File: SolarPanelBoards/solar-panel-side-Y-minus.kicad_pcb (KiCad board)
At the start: 2 copper layers, 82 x 99 mm, 24 parts, among them J1 Conn_01x06, U1 OPT3001DNPT

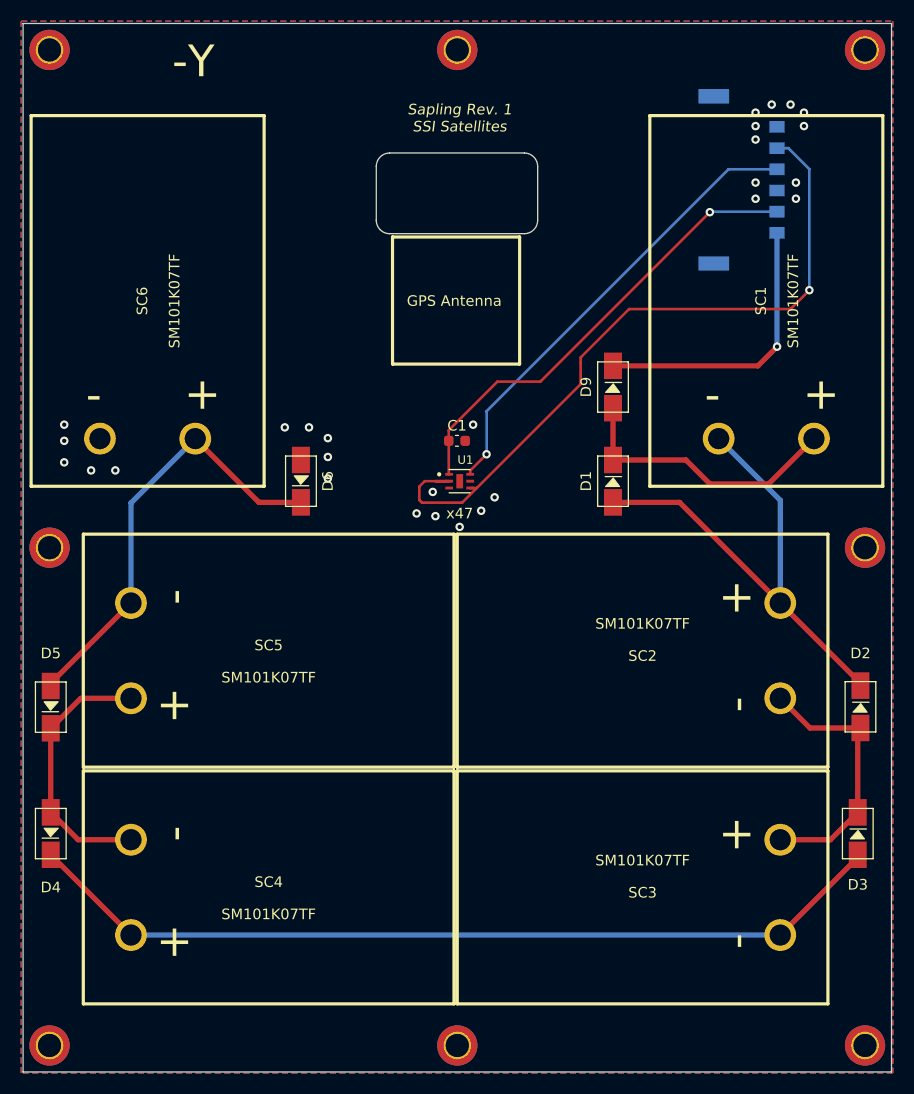
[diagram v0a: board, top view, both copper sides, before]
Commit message: Battery board and side panels ready for CAD check and review, pycubed not finished yet
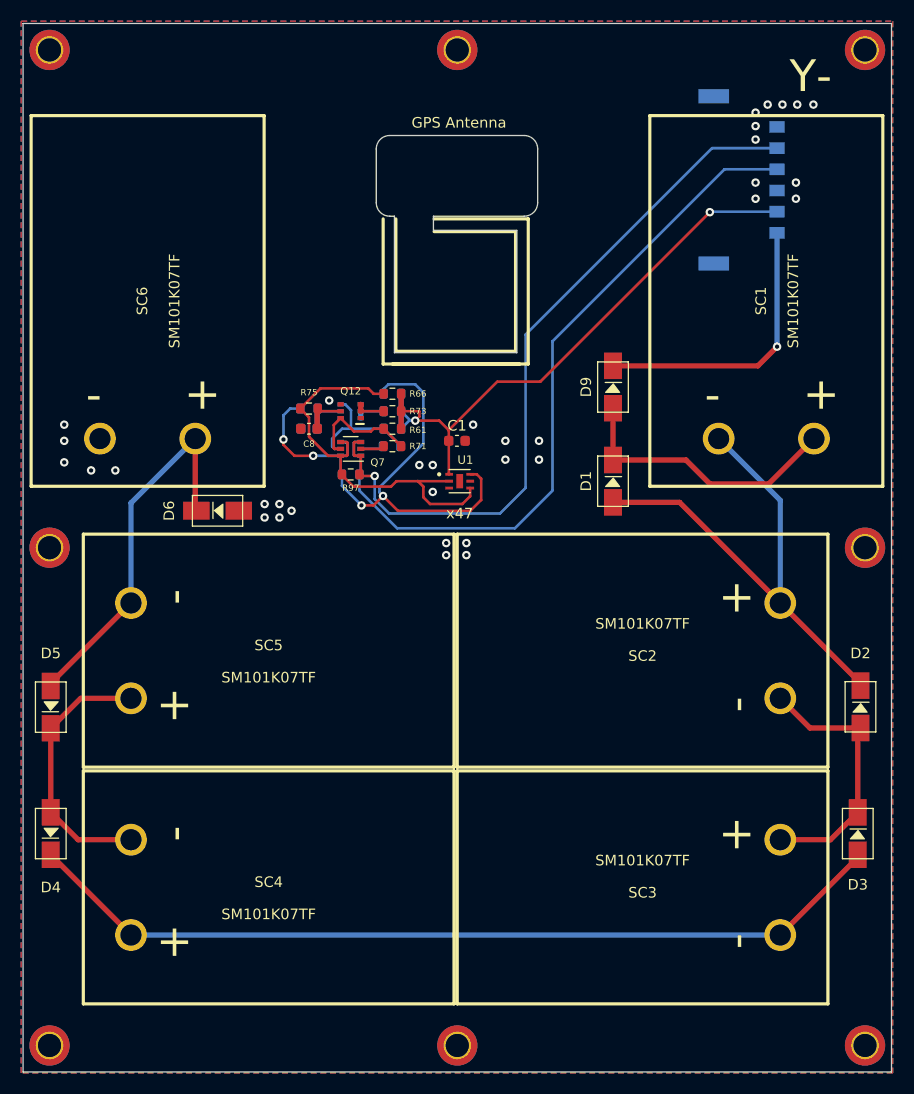
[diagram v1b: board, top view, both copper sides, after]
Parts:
- added C40: 10nF, Capacitor_SMD:C_0603_1608Metric, B.Cu at (133.3, 86.0)
- added C8: 10nF, Capacitor_SMD:C_0603_1608Metric, F.Cu at (133.3, 86.0)
- added Q12: BSS138DWQ-7, sapling:BSS138DWQ-7, F.Cu at (137.3, 84.3)
- added Q13: BSS138DWQ-7, sapling:BSS138DWQ-7, B.Cu at (137.3, 84.3)
- added Q7: MBT2222ADW1T1, Package_TO_SOT_SMD:SOT-363_SC-70-6, F.Cu at (137.3, 87.9)
- added Q8: MBT2222ADW1T1, Package_TO_SOT_SMD:SOT-363_SC-70-6, B.Cu at (137.3, 87.9)
- added R61: 10K, Resistor_SMD:R_0603_1608Metric, F.Cu at (141.2, 86.0)
- added R62: 10K, Resistor_SMD:R_0603_1608Metric, B.Cu at (141.2, 86.0)
- added R66: 10K, Resistor_SMD:R_0603_1608Metric, F.Cu at (141.2, 82.7)
- added R67: 10K, Resistor_SMD:R_0603_1608Metric, B.Cu at (141.2, 82.7)
- added R71: 680, Resistor_SMD:R_0603_1608Metric, F.Cu at (141.2, 87.6)
- added R72: 680, Resistor_SMD:R_0603_1608Metric, B.Cu at (141.2, 87.6)
- added R73: 100K, Resistor_SMD:R_0603_1608Metric, F.Cu at (141.2, 84.3)
- added R74: 100K, Resistor_SMD:R_0603_1608Metric, B.Cu at (141.2, 84.3)
- added R75: 200K, Resistor_SMD:R_0603_1608Metric, F.Cu at (133.3, 84.1)
- added R76: 200K, Resistor_SMD:R_0603_1608Metric, B.Cu at (133.3, 84.1)
- added R97: 0, Resistor_SMD:R_0603_1608Metric, F.Cu at (137.3, 90.3)
- added R98: 0, Resistor_SMD:R_0603_1608Metric, B.Cu at (137.3, 90.3)
- added REF**: AP.12F_Taoglas, sapling:AP.12F_Taoglas, F.Cu at (147.7, 64.9)
- moved D6 8.36 mm to (124.7, 93.7), turned to 0 degrees
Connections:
- U1 pad 2: SCL -> SCL_SUN
- U1 pad 4: SCL -> SCL_SUN
- U1 pad 6: SDA -> SDA_SUN
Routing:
- net SDA_SUN: track 0.00 -> 50.7 mm, vias 0 -> 4
- net SCL_SUN: track 0.00 -> 38.3 mm
- net SDA: track 43.5 -> 69.0 mm, vias 1 -> 0
- net +3V3: track 43.7 -> 60.0 mm, vias 1 -> 2
- net Net-(Q13-Pad6): track 0.00 -> 12.2 mm
- net Net-(Q12-Pad6): track 0.00 -> 10.8 mm
- net Net-(D5-Pad2): track 41.5 -> 35.9 mm
- net Net-(C8-Pad1): track 0.00 -> 4.19 mm
- net Net-(C40-Pad1): track 0.00 -> 4.19 mm
- net Net-(Q12-Pad2): track 0.00 -> 2.81 mm
- net Net-(Q13-Pad2): track 0.00 -> 2.81 mm
- net Net-(Q7-Pad2): track 0.00 -> 2.27 mm
- net Net-(Q8-Pad2): track 0.00 -> 2.20 mm
- net SCL: track 68.2 -> 69.3 mm
- net GND: vias 28 -> 34
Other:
- outline, holes or cut-outs redrawn
- board text added: "+3.3V"
- board text removed: "3.3"
- board text removed: "Sapling Rev. 1 SSI Satellites"

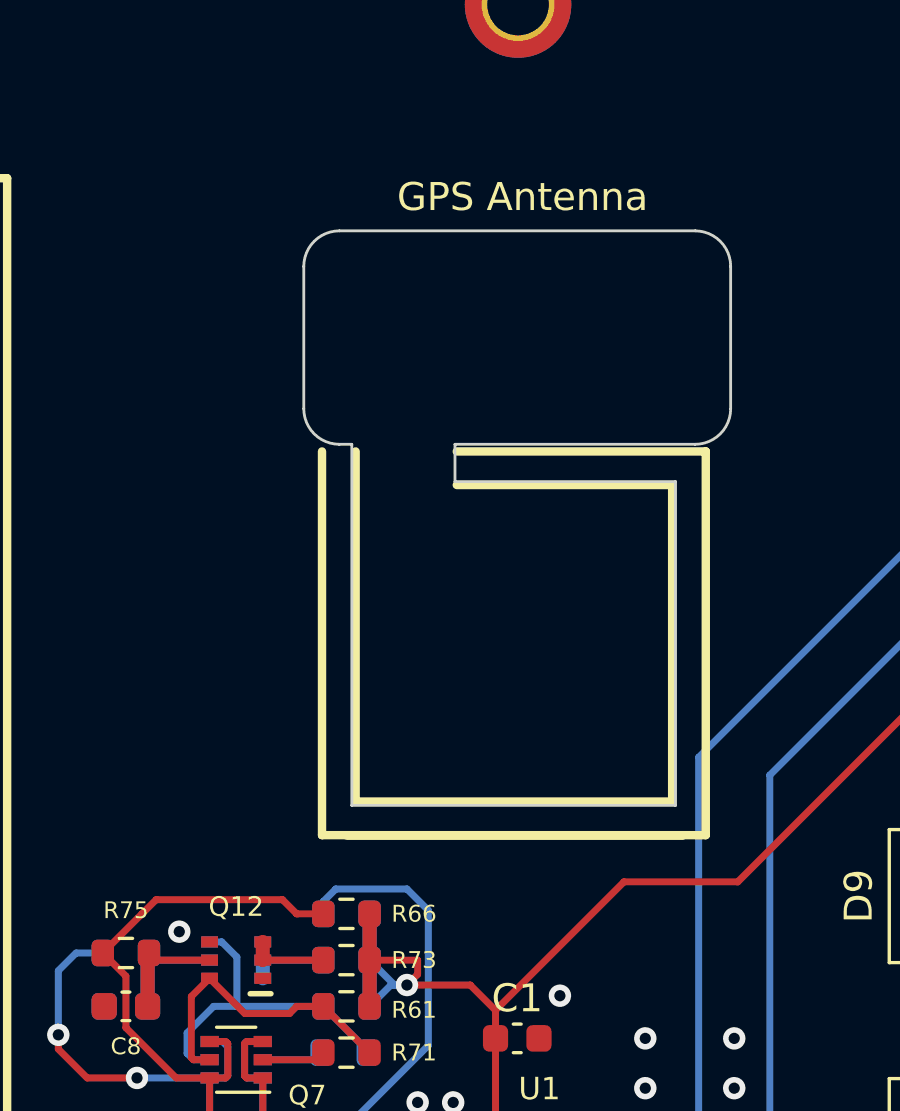
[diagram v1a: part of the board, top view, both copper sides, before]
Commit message: side panels ready except for RF trace width
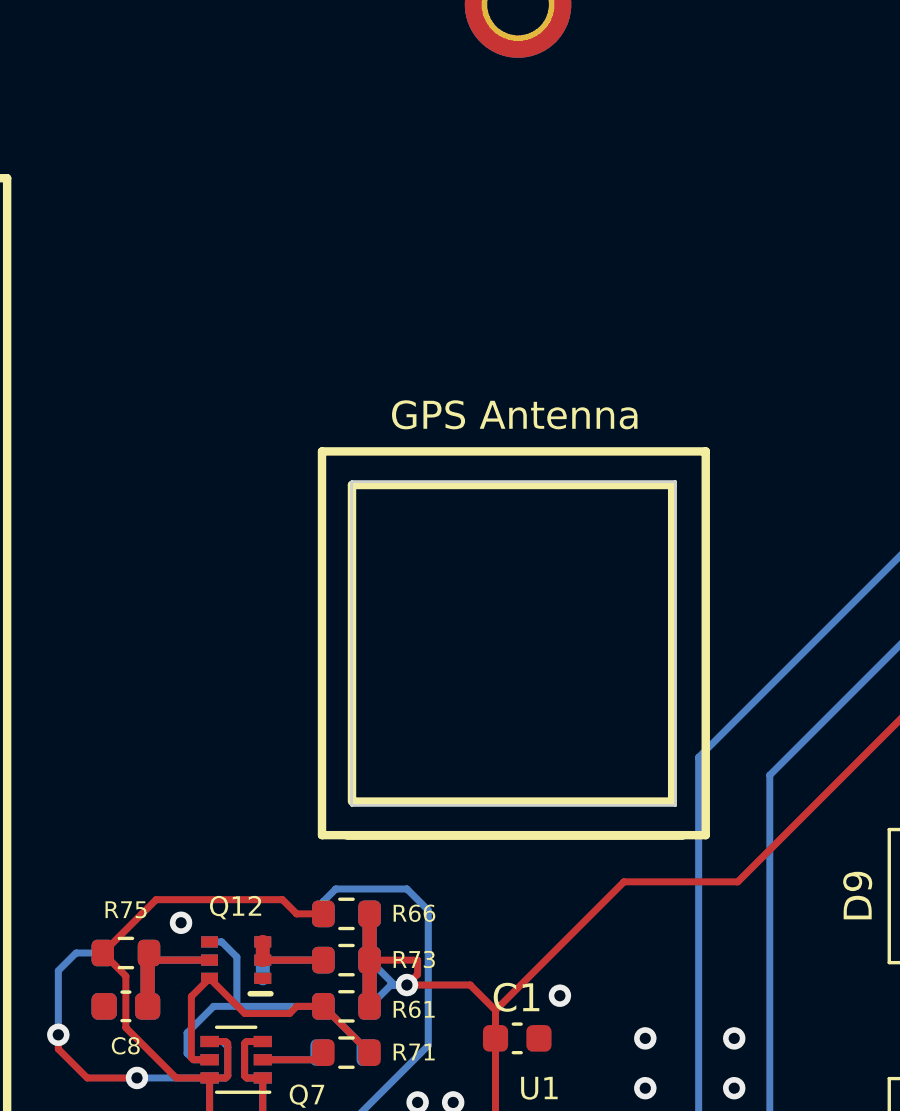
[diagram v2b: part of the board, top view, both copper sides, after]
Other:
- outline, holes or cut-outs redrawn
